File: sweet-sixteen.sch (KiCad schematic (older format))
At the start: 81 parts, among them P1 SDA_I, P10 VIN_O, P11 GND_O, P12 SDA_O, P13 CLK_O, P14 LE_O, P15 ~OE_O, P2 CLK_I, P3 LE_I, P4 ~OE_I, P5 CONN_02X20, P6 5V_I, P7 VIN_I, P8 GND_I, P9 5V_O, U1 OKI-T/3-W40, U10 STP16CPC26, U11 STP16CPC26, U12 STP16CPC26, U13 74HCT08, U2 STP16CPC26, U3 OKI-T/3-W40, U4 STP16CPC26, U5 74HCT08, U6 STP16CPC26, U7 STP16CPC26, U8 STP16CPC26, U9 STP16CPC26

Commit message: basic pcb placement
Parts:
- AFF1, AFF2, AFF3, AFF4, AFF5, AFF6, AFF7, AFF8: footprint (none) -> 16segments:PSA12-11
- CON_PWR1: footprint (none) -> Connect:BARREL_JACK
- U1, U3: footprint (none) -> oki-t3:OKI-T3
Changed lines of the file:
@@
 F 0 "AFF1" H 3050 7400 50  0000 C CNN
 F 1 "16SEGMENTS" H 3075 5650 50  0000 C CNN
-F 2 "" H 3070 6475 50  0001 C CNN
+F 2 "16segments:PSA12-11" H 3070 6475 50  0001 C CNN
 F 3 "" H 3070 6475 50  0000 C CNN
 	1    3050 6500
@@
 F 0 "AFF2" H 4900 7400 50  0000 C CNN
 F 1 "16SEGMENTS" H 4925 5650 50  0000 C CNN
-F 2 "" H 4920 6475 50  0001 C CNN
+F 2 "16segments:PSA12-11" H 4920 6475 50  0001 C CNN
 F 3 "" H 4920 6475 50  0000 C CNN
 	1    4900 6500
@@
 F 0 "AFF3" H 6750 7400 50  0000 C CNN
 F 1 "16SEGMENTS" H 6775 5650 50  0000 C CNN
-F 2 "" H 6770 6475 50  0001 C CNN
+F 2 "16segments:PSA12-11" H 6770 6475 50  0001 C CNN
 F 3 "" H 6770 6475 50  0000 C CNN
 	1    6750 6500
@@
 F 0 "AFF4" H 8600 7400 50  0000 C CNN
 F 1 "16SEGMENTS" H 8625 5650 50  0000 C CNN
-F 2 "" H 8620 6475 50  0001 C CNN
+F 2 "16segments:PSA12-11" H 8620 6475 50  0001 C CNN
 F 3 "" H 8620 6475 50  0000 C CNN
 	1    8600 6500
@@
 F 0 "AFF5" H 10750 7400 50  0000 C CNN
 F 1 "16SEGMENTS" H 10775 5650 50  0000 C CNN
-F 2 "" H 10770 6475 50  0001 C CNN
+F 2 "16segments:PSA12-11" H 10770 6475 50  0001 C CNN
 F 3 "" H 10770 6475 50  0000 C CNN
 	1    10750 6500
@@
 F 0 "AFF6" H 12600 7400 50  0000 C CNN
 F 1 "16SEGMENTS" H 12625 5650 50  0000 C CNN
-F 2 "" H 12620 6475 50  0001 C CNN
+F 2 "16segments:PSA12-11" H 12620 6475 50  0001 C CNN
 F 3 "" H 12620 6475 50  0000 C CNN
 	1    12600 6500
@@
 F 0 "AFF7" H 14450 7400 50  0000 C CNN
 F 1 "16SEGMENTS" H 14475 5650 50  0000 C CNN
-F 2 "" H 14470 6475 50  0001 C CNN
+F 2 "16segments:PSA12-11" H 14470 6475 50  0001 C CNN
 F 3 "" H 14470 6475 50  0000 C CNN
 	1    14450 6500
@@
 F 0 "AFF8" H 16300 7400 50  0000 C CNN
 F 1 "16SEGMENTS" H 16325 5650 50  0000 C CNN
-F 2 "" H 16320 6475 50  0001 C CNN
+F 2 "16segments:PSA12-11" H 16320 6475 50  0001 C CNN
 F 3 "" H 16320 6475 50  0000 C CNN
 	1    16300 6500
@@
 F 0 "CON_PWR1" H 5800 3200 50  0000 C CNN
 F 1 "PWR" H 5800 2750 50  0000 C CNN
-F 2 "" H 5800 2950 50  0001 C CNN
+F 2 "Connect:BARREL_JACK" H 5800 2950 50  0001 C CNN
 F 3 "" H 5800 2950 50  0000 C CNN
 	1    5800 2950
@@
 F 0 "U1" H 1500 2300 60  0000 C CNN
 F 1 "OKI-T/3-W40" H 1500 2450 60  0000 C CNN
-F 2 "" H 1500 2450 60  0001 C CNN
+F 2 "oki-t3:OKI-T3" H 1500 2450 60  0001 C CNN
 F 3 "" H 1500 2450 60  0000 C CNN
 	1    1500 2450
@@
 F 0 "U3" H 3750 2300 60  0000 C CNN
 F 1 "OKI-T/3-W40" H 3750 2450 60  0000 C CNN
-F 2 "" H 3750 2450 60  0001 C CNN
+F 2 "oki-t3:OKI-T3" H 3750 2450 60  0001 C CNN
 F 3 "" H 3750 2450 60  0000 C CNN
 	1    3750 2450

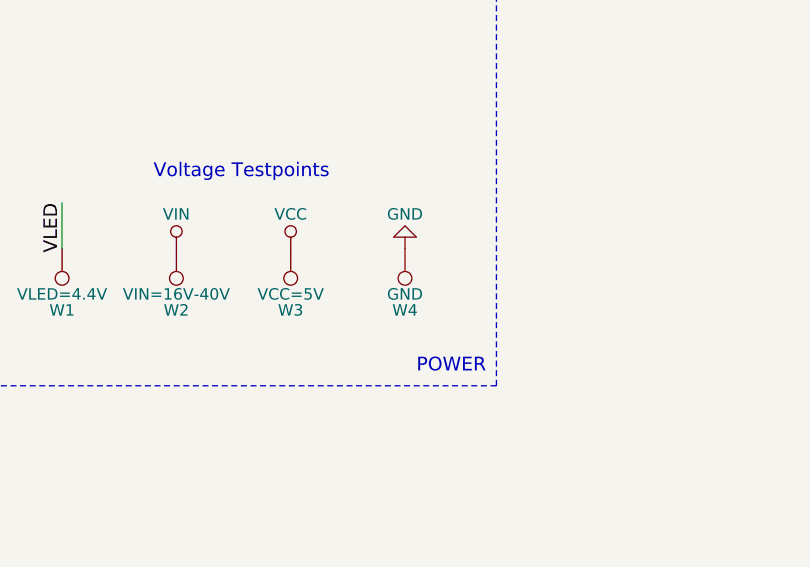
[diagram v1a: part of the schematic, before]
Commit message: add more gnd-testpoints, move testpoint-labels to silkscreen
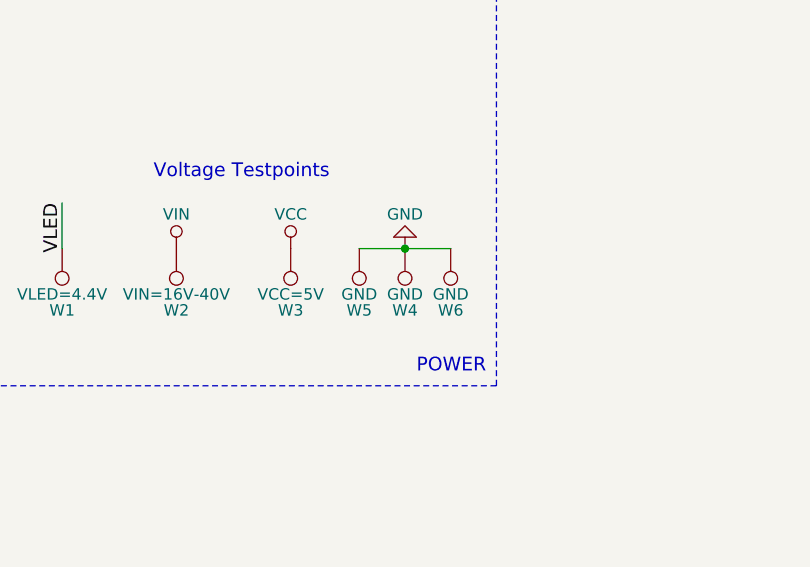
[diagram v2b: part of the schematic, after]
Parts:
- added W5, W6: GND, Measurement_Points:Measurement_Point_Round-SMD-Pad_Big, symbol TEST_1P
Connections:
- net GND: now also W5.1, W6.1

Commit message: redo pcb, footprints, pi interface
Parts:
- P1, P10, P11, P12, P13, P14, P15, P2, P3, P4, P6, P7, P8, P9: footprint SMD_Packages:1Pin -> Measurement_Points:Measurement_Point_Square-SMD-Pad_Big
- P5: footprint Pin_Headers:Pin_Header_Straight_2x20 -> rpi-header:rpi-header
- U1: renamed from U2; footprint SMD_Packages:SOIC-24 -> chips:STP16CPC26MTR
- U2: renamed from U4; footprint SMD_Packages:SOIC-24 -> chips:STP16CPC26MTR
- U3: renamed from U6; footprint SMD_Packages:SOIC-24 -> chips:STP16CPC26MTR
- U30: renamed from U5; footprint SMD_Packages:SOIC-14_N -> chips:SN74HCT08D
- U31: renamed from U13; footprint SMD_Packages:SOIC-14_N -> chips:SN74HCT08D
- U4: renamed from U7; footprint SMD_Packages:SOIC-24 -> chips:STP16CPC26MTR
- U5: renamed from U8; footprint SMD_Packages:SOIC-24 -> chips:STP16CPC26MTR
- U6: renamed from U9; footprint SMD_Packages:SOIC-24 -> chips:STP16CPC26MTR
- U7: renamed from U10; footprint SMD_Packages:SOIC-24 -> chips:STP16CPC26MTR
- U8: renamed from U11; footprint SMD_Packages:SOIC-24 -> chips:STP16CPC26MTR
- U9: renamed from U12; footprint SMD_Packages:SOIC-24 -> chips:STP16CPC26MTR
- renumbered C3 to C1, C4 to C2, C5 to C3, C1 to C30, C2 to C31, C6 to C4, C7 to C5, C8 to C6, C9 to C7, C10 to C8, C11 to C9, F1 to F20, F3 to F21, F2 to F30, R10 to R20, R11 to R21, R12 to R22, R13 to R23, U1 to U20, U3 to U21

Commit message: move footprints to inch locations, fix outline, lock footprints
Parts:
- removed JP5: JUMPER, jumper:SMD_Jumper_2, symbol JUMPER
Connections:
- net SDA: no longer P1.1 (P1), U1.2 (SDI)
- net VIN: now also CON_PWR1.1
- net SDA_12: now reaches U1.22 (SDO), U2.2 (SDI)
- net SD23: now reaches U2.22 (SDO), U3.2 (SDI)
- net SDA_34: now reaches U3.22 (SDO), U4.2 (SDI)
- net SDA_45: now reaches U4.22 (SDO), U5.2 (SDI)
- net SDA_67: now reaches U6.22 (SDO), U7.2 (SDI)
- net SDA_78: now reaches U7.22 (SDO), U8.2 (SDI)
- net SDA_56: now reaches U5.22 (SDO), U6.2 (SDI)
- net SDA_89: now reaches U8.22 (SDO), U9.2 (SDI)
- net SDA_O: now reaches U31.1, U31.2, U9.22 (SDO)
- new net SDA_I: P1.1 (P1), U1.2 (SDI)
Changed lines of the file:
@@
 LE
 Text Label 1750 8850 0    60   ~ 0
-SDA
+SDA_I
 Text Label 7550 14100 2    60   ~ 0
 SDA
@@
 L VIN #PWR056
 U 1 1 58AFC302
-P 6100 2000
-F 0 "#PWR056" H 6100 1850 50  0001 C CNN
-F 1 "VIN" H 6100 2150 50  0000 C CNN
-F 2 "" H 6100 2000 50  0000 C CNN
-F 3 "" H 6100 2000 50  0000 C CNN
-	1    6100 2000
+P 6100 2600
+F 0 "#PWR056" H 6100 2450 50  0001 C CNN
+F 1 "VIN" H 6100 2750 50  0000 C CNN
+F 2 "" H 6100 2600 50  0000 C CNN
+F 3 "" H 6100 2600 50  0000 C CNN
+	1    6100 2600
 	1    0    0    -1
 $EndComp
@@
 $EndComp
 $Comp
-L JUMPER JP5
-U 1 1 58B035F8
-P 6100 2400
-F 0 "JP5" H 6100 2550 50  0000 C CNN
-F 1 "JUMPER" H 6100 2320 50  0000 C CNN
-F 2 "jumper:SMD_Jumper_2" H 6100 2400 50  0001 C CNN
-F 3 "" H 6100 2400 50  0000 C CNN
-	1    6100 2400
-	0    -1   -1   0
-$EndComp
-$Comp
 L TEST_1P W2
 U 1 1 5850D464
@@
 	3250 13250 3250 13050
 Wire Wire Line
-	6100 2700 6100 2850
+	6100 2600 6100 2850
 Wire Wire Line
 	3850 13150 3850 13250
@@
 L PWR_FLAG #FLG074
 U 1 1 58B37130
-P 6150 2100
-F 0 "#FLG074" H 6150 2195 50  0001 C CNN
-F 1 "PWR_FLAG" H 6150 2280 50  0000 C CNN
-F 2 "" H 6150 2100 50  0000 C CNN
-F 3 "" H 6150 2100 50  0000 C CNN
-	1    6150 2100
+P 6150 2700
+F 0 "#FLG074" H 6150 2795 50  0001 C CNN
+F 1 "PWR_FLAG" H 6150 2880 50  0000 C CNN
+F 2 "" H 6150 2700 50  0000 C CNN
+F 3 "" H 6150 2700 50  0000 C CNN
+	1    6150 2700
 	0    1    1    0
 $EndComp
@@
 Connection ~ 6100 3150
 Wire Wire Line
-	6150 2100 6100 2100
-Wire Wire Line
-	6100 2100 6100 2000
-Connection ~ 6100 2100
+	6150 2700 6100 2700
+Connection ~ 6100 2700
 Wire Wire Line
 	7450 8400 7500 8400
@@
 	8500 3000 8900 3000
 Connection ~ 8700 3000
+Text Label 3550 8850 0    60   ~ 0
+SDA_12
+Text Label 5400 8850 0    60   ~ 0
+SD23
+Text Label 7250 8850 0    60   ~ 0
+SDA_34
+Text Label 9100 8850 0    60   ~ 0
+SDA_45
+Text Label 11250 8850 0    60   ~ 0
+SDA_56
+Text Label 13100 8850 0    60   ~ 0
+SDA_67
+Text Label 14950 8850 0    60   ~ 0
+SDA_78
+Text Label 16800 8850 0    60   ~ 0
+SDA_89
+Text Label 18600 8850 0    60   ~ 0
+SDA_O
 $EndSCHEMATC

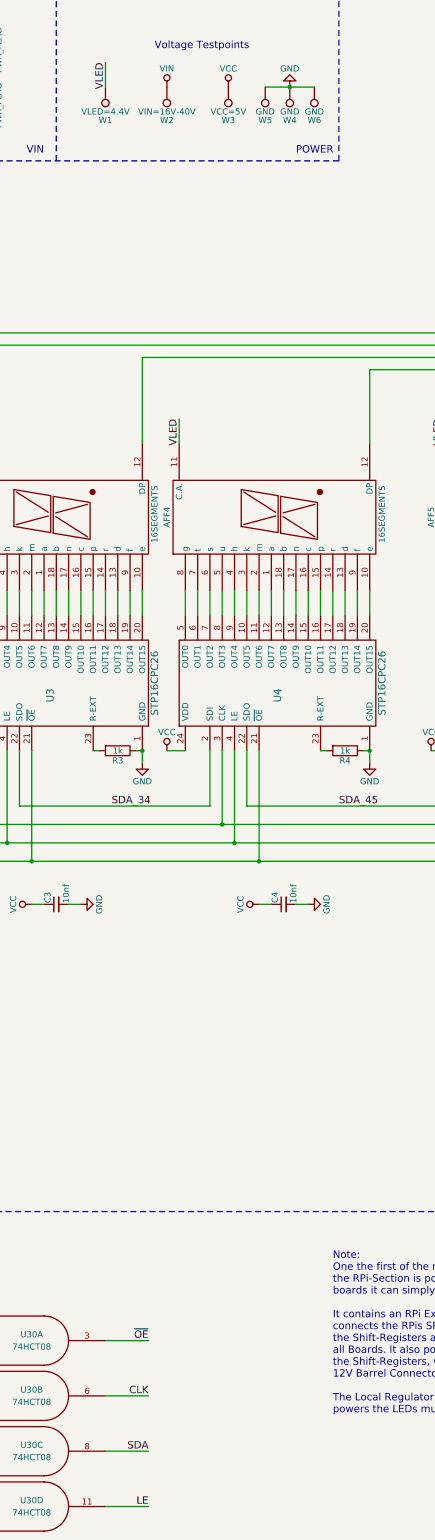
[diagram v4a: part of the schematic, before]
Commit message: More Power traces
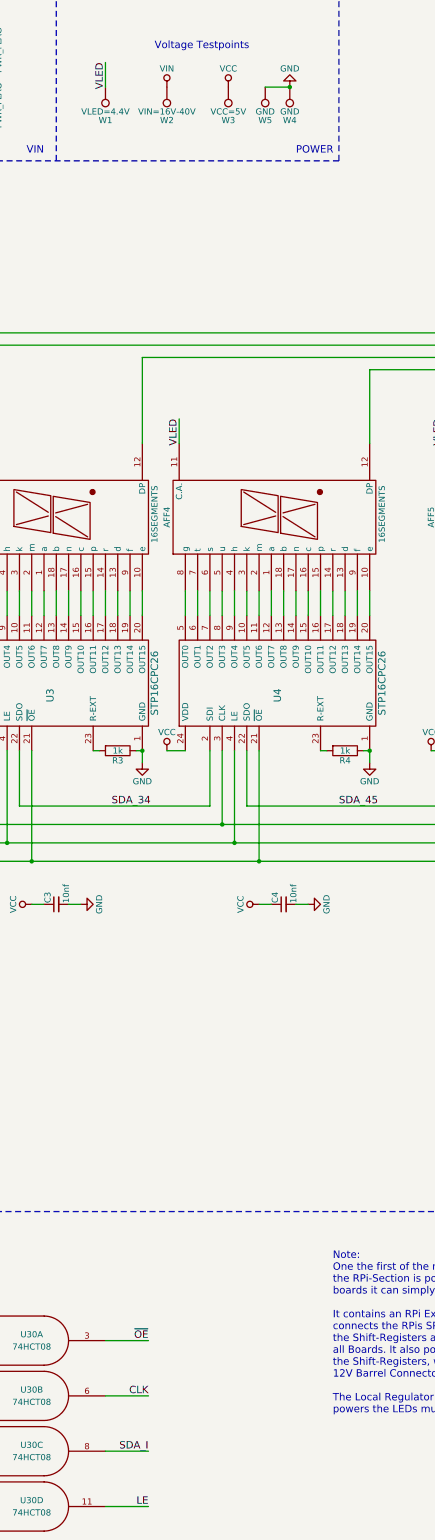
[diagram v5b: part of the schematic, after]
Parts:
- removed W6: GND, Measurement_Points:Measurement_Point_Round-SMD-Pad_Big, symbol TEST_1P
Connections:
- net SDA is gone; now on net SDA_I: U30.8
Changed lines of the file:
@@
 SDA_I
 Text Label 7550 14100 2    60   ~ 0
-SDA
+SDA_I
 Text Label 7550 13650 2    60   ~ 0
 CLK
@@
 	6800 3600 6800 450
 $Comp
-L TEST_1P W6
-U 1 1 58AC0293
-P 8900 3000
-F 0 "W6" H 8900 3270 50  0000 C CNN
-F 1 "GND" H 8900 3200 50  0000 C CNN
-F 2 "Measurement_Points:Measurement_Point_Round-SMD-Pad_Big" H 9100 3000 50  0001 C CNN
-F 3 "" H 9100 3000 50  0000 C CNN
-	1    8900 3000
-	-1   0    0    1
-$EndComp
-$Comp
 L TEST_1P W5
 U 1 1 58AC03B7
@@
 	-1   0    0    1
 $EndComp
-Wire Wire Line
-	8500 3000 8900 3000
 Connection ~ 8700 3000
 Text Label 3550 8850 0    60   ~ 0
@@
 Text Label 18600 8850 0    60   ~ 0
 SDA_O
+Wire Wire Line
+	8500 3000 8700 3000
 $EndSCHEMATC

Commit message: all done but GND
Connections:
- net at AFF1.12 (DP): now also U9.10 (OUT5); no longer U9.12 (OUT7)
- net at AFF2.12 (DP): now also U9.9 (OUT4); no longer U9.11 (OUT6)
- net at AFF3.12 (DP): now also U9.8 (OUT3); no longer U9.10 (OUT5)
- net at AFF4.12 (DP): now also U9.11 (OUT6); no longer U9.9 (OUT4)
- net at AFF5.12 (DP): now also U9.12 (OUT7); no longer U9.8 (OUT3)
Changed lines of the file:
@@
 	11500 5900 11500 5400
 Wire Wire Line
-	11500 5400 17650 5400
-Wire Wire Line
-	17650 5400 17650 7300
-Wire Wire Line
-	17750 7300 17750 5300
-Wire Wire Line
-	17750 5300 9350 5300
+	11500 5400 18050 5400
+Wire Wire Line
+	9350 5300 17950 5300
 Wire Wire Line
 	9350 5300 9350 5900
@@
 	7500 5900 7500 5200
 Wire Wire Line
-	7500 5200 17850 5200
-Wire Wire Line
-	17850 5200 17850 7300
-Wire Wire Line
-	17950 7300 17950 5100
-Wire Wire Line
-	17950 5100 5650 5100
-Wire Wire Line
 	5650 5100 5650 5900
 Wire Wire Line
 	3800 5900 3800 5000
-Wire Wire Line
-	3800 5000 18050 5000
-Wire Wire Line
-	18050 5000 18050 7300
 Wire Wire Line
 	18250 5200 20100 5200
@@
 Wire Wire Line
 	8500 3000 8700 3000
+Wire Wire Line
+	17750 7300 17750 5100
+Wire Wire Line
+	17750 5100 5650 5100
+Wire Wire Line
+	3800 5000 17850 5000
+Wire Wire Line
+	18050 5400 18050 7300
+Wire Wire Line
+	17950 5300 17950 7300
+Wire Wire Line
+	17850 5000 17850 7300
+Wire Wire Line
+	17650 5200 17650 7300
+Wire Wire Line
+	7500 5200 17650 5200
 $EndSCHEMATC

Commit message: re-route things with more care
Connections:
- net SDA_O: now also P12.1 (P1), U31.3; no longer U31.1, U31.2, U9.22 (SDO)
- net CLK_O: now reaches P13.1 (P1), U31.6
- net LE_O: now reaches P14.1 (P1), U31.8
- net ~OE_O: now reaches P15.1 (P1), U31.11
- net SD23 renamed SD_23
- new net SDA_9O: U31.1, U31.2, U9.22 (SDO)
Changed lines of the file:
@@
 SDA_12
 Text Label 5400 8850 0    60   ~ 0
-SD23
+SD_23
 Text Label 7250 8850 0    60   ~ 0
 SDA_34
@@
 SDA_89
 Text Label 18600 8850 0    60   ~ 0
-SDA_O
+SDA_9O
 Wire Wire Line
 	8500 3000 8700 3000
@@
 Wire Wire Line
 	7500 5200 17650 5200
+Text Label 21050 8400 0    60   ~ 0
+SDA_O
+Text Label 21050 8850 0    60   ~ 0
+CLK_O
+Text Label 21050 9300 0    60   ~ 0
+LE_O
+Text Label 21050 9750 0    60   ~ 0
+~OE_O
 $EndSCHEMATC

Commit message: re-route all
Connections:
- net at AFF1.12 (DP): now also U9.8 (OUT3); no longer U9.10 (OUT5)
- net at AFF3.12 (DP): now also U9.10 (OUT5); no longer U9.8 (OUT3)
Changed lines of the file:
@@
 	8500 3000 8700 3000
-Wire Wire Line
-	17750 7300 17750 5100
-Wire Wire Line
-	17750 5100 5650 5100
-Wire Wire Line
-	3800 5000 17850 5000
 Wire Wire Line
 	18050 5400 18050 7300
 Wire Wire Line
 	17950 5300 17950 7300
-Wire Wire Line
-	17850 5000 17850 7300
-Wire Wire Line
-	17650 5200 17650 7300
-Wire Wire Line
-	7500 5200 17650 5200
 Text Label 21050 8400 0    60   ~ 0
 SDA_O
@@
 Text Label 21050 9750 0    60   ~ 0
 ~OE_O
+Wire Wire Line
+	17650 7300 17650 5000
+Wire Wire Line
+	17650 5000 3800 5000
+Wire Wire Line
+	17750 7300 17750 5100
+Wire Wire Line
+	17750 5100 5650 5100
+Wire Wire Line
+	17850 7300 17850 5200
+Wire Wire Line
+	17850 5200 7500 5200
 $EndSCHEMATC
